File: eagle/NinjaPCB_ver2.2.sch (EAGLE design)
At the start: 58 parts, among them IC3 ANALOGSW_AD_SOT23-6, IC6 NAU7802, J2 ATX24, J3 HEATER, J4 HEATER_TEMP, Q1 S8550, Q2 IRF520NPBF, Q3 IRF520NPBF, Q4 S8550, Q5 IRF520NPBF, Q6 S8550, Q7 S8550, Q8 S8550, U1 CJT1117-3.3-SOT223

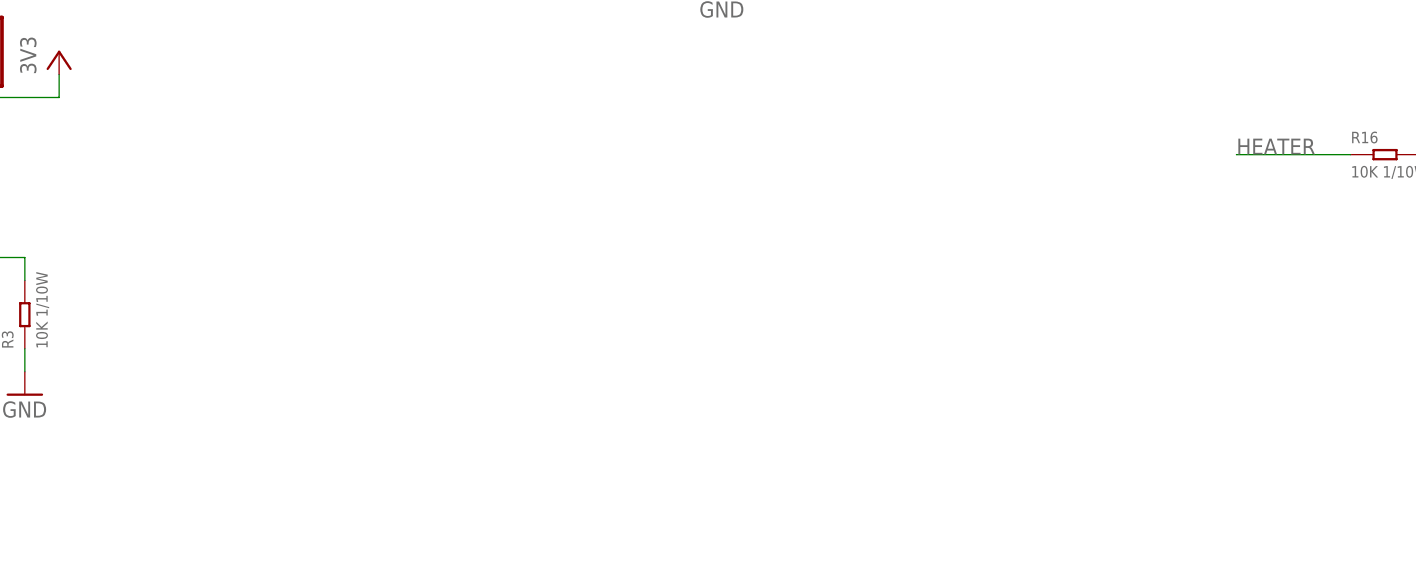
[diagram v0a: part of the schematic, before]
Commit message: changed R14 into RT. no reason for T
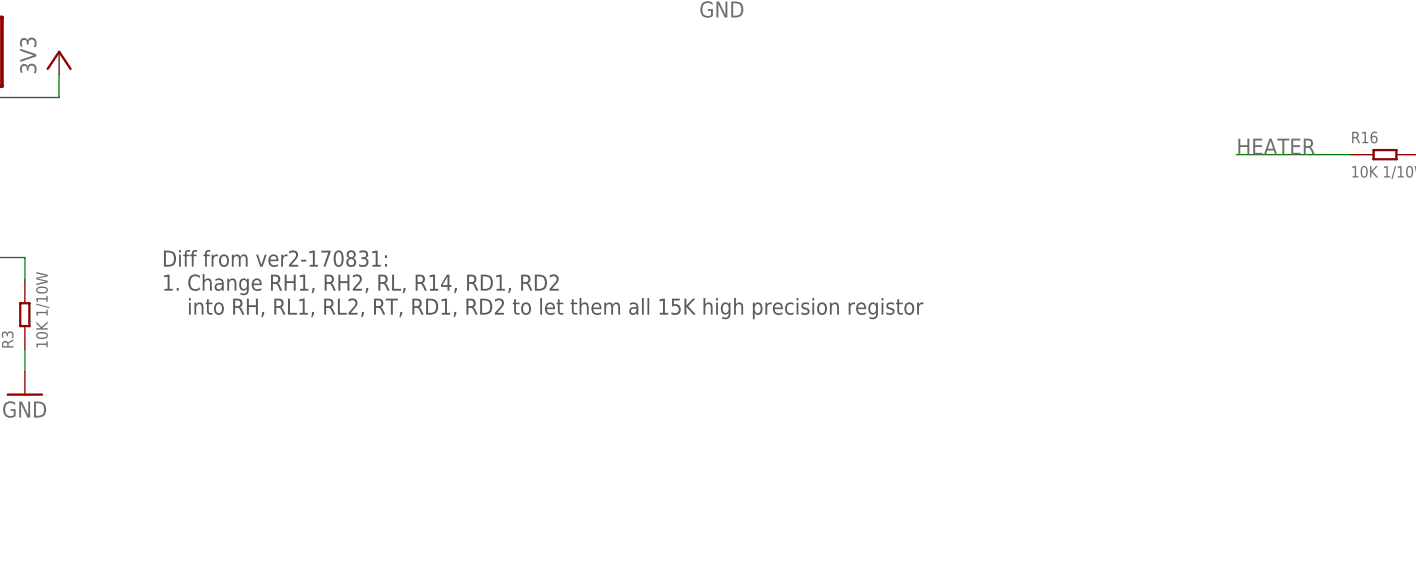
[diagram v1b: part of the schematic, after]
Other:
- note added: "Diff from ver2-170831: 1. Change RH1, RH2, RL, R14, RD1, RD2 into RH, RL1, RL2, RT, RD1, RD2 to let them all 15K high precision registor"
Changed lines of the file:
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@@
 <setting verticaltext="up"/>
 </settings>
-<grid distance="0.05" unitdist="inch" unit="inch" style="lines" multiple="1" display="no" altdistance="0.01" altunitdist="inch" altunit="inch"/>
+<grid distance="0.1" unitdist="inch" unit="inch" style="lines" multiple="1" display="no" altdistance="0.01" altunitdist="inch" altunit="inch"/>
 <layers>
 <layer number="1" name="Top" color="4" fill="1" visible="no" active="no"/>
@@
 <text x="26.67" y="238.76" size="3.81" layer="97">MCU</text>
 <text x="24.13" y="68.58" size="3.81" layer="97">POWER</text>
+<text x="167.64" y="91.44" size="1.778" layer="97">Diff from ver2-170831:
+1. Change RH1, RH2, RL, R14, RD1, RD2
+    into RH, RL1, RL2, RT, RD1, RD2 to let them all 15K high precision registor</text>
 </plain>
 <instances>
@@
 </schematic>
 </drawing>
+<compatibility>
+<note version="6.3" minversion="6.2.2" severity="warning">
+Since Version 6.2.2 text objects can contain more than one line,
+which will not be processed correctly with this version.
+</note>
+</compatibility>
 </eagle>

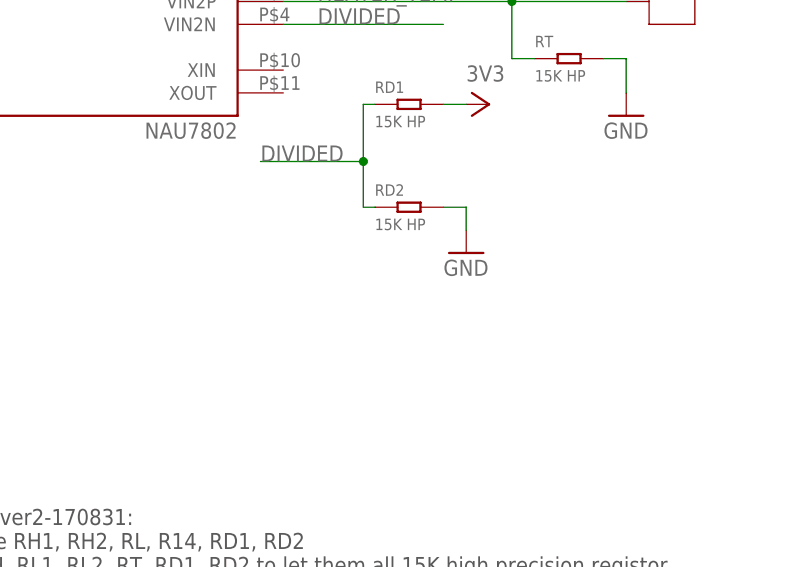
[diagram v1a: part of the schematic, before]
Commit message: add low ESR cap to standard voltage for NAU7802
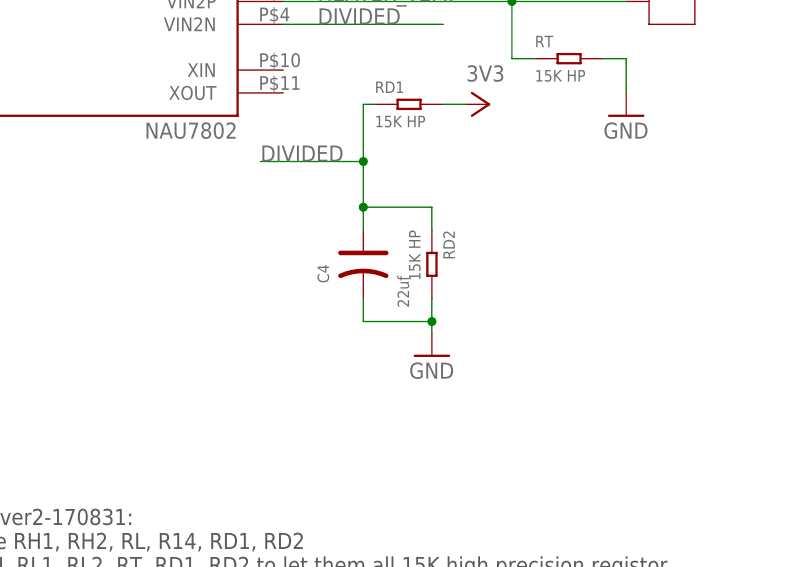
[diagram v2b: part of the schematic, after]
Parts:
- added C4: 22uf, Seeed-Capacitor:TANTALUM-SMD-22UF-16V(AVX-B)
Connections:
- net DIVIDED: now also C4.+
- net GND: now also C4.-
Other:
- moved on the sheet: RD2
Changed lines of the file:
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@@
 <setting verticaltext="up"/>
 </settings>
-<grid distance="0.1" unitdist="inch" unit="inch" style="lines" multiple="1" display="no" altdistance="0.01" altunitdist="inch" altunit="inch"/>
+<grid distance="0.05" unitdist="inch" unit="inch" style="lines" multiple="1" display="no" altdistance="0.01" altunitdist="inch" altunit="inch"/>
 <layers>
 <layer number="1" name="Top" color="4" fill="1" visible="no" active="no"/>
@@
 <part name="C1" library="Seeed-Capacitor" deviceset="CERAMIC-100NF-50V-10%-X7R(0603)" device="" value="100nf"/>
 <part name="RL1" library="PCR-RCL" deviceset="R0603" device="" value="15K HP"/>
+<part name="C4" library="Seeed-Capacitor" deviceset="TANTALUM-SMD-22UF-16V(AVX-B)" device="" value="22uf"/>
 </parts>
 <sheets>
@@
 <instance part="P+10" gate="VCC" x="214.63" y="177.8"/>
 <instance part="P+12" gate="VCC" x="232.41" y="143.51" rot="R270"/>
-<instance part="GND13" gate="1" x="229.87" y="127"/>
+<instance part="GND13" gate="1" x="226.06" y="115.57"/>
 <instance part="RD1" gate="G$1" x="223.52" y="143.51"/>
-<instance part="RD2" gate="G$1" x="223.52" y="132.08"/>
+<instance part="RD2" gate="G$1" x="226.06" y="125.73" rot="R270"/>
 <instance part="GND15" gate="1" x="160.02" y="135.89"/>
 <instance part="C3" gate="G$1" x="160.02" y="154.94" rot="R90"/>
@@
 <instance part="C1" gate="G$1" x="43.18" y="209.55"/>
 <instance part="RL1" gate="G$1" x="199.39" y="224.79"/>
+<instance part="C4" gate="G$1" x="218.44" y="125.73" smashed="yes" rot="R270">
+<attribute name="NAME" x="213.36" y="125.73" size="1.27" layer="95" ratio="10" rot="R270"/>
+<attribute name="VALUE" x="222.25" y="124.46" size="1.27" layer="96" ratio="10" rot="R270"/>
+</instance>
 </instances>
 <busses>
@@
 <segment>
 <pinref part="GND13" gate="1" pin="GND"/>
-<wire x1="229.87" y1="132.08" x2="229.87" y2="129.54" width="0.1524" layer="91"/>
 <pinref part="RD2" gate="G$1" pin="2"/>
-<wire x1="227.33" y1="132.08" x2="229.87" y2="132.08" width="0.1524" layer="91"/>
+<wire x1="226.06" y1="121.92" x2="226.06" y2="119.38" width="0.1524" layer="91"/>
+<pinref part="C4" gate="G$1" pin="-"/>
+<wire x1="226.06" y1="119.38" x2="226.06" y2="118.11" width="0.1524" layer="91"/>
+<wire x1="226.06" y1="119.38" x2="218.44" y2="119.38" width="0.1524" layer="91"/>
+<wire x1="218.44" y1="119.38" x2="218.44" y2="121.92" width="0.1524" layer="91"/>
+<junction x="226.06" y="119.38"/>
 </segment>
 <segment>
@@
 <label x="207.01" y="137.16" size="1.778" layer="95"/>
 <pinref part="RD2" gate="G$1" pin="1"/>
-<wire x1="219.71" y1="132.08" x2="218.44" y2="132.08" width="0.1524" layer="91"/>
-</segment>
-<segment>
+<wire x1="226.06" y1="129.54" x2="226.06" y2="132.08" width="0.1524" layer="91"/>
+<wire x1="226.06" y1="132.08" x2="218.44" y2="132.08" width="0.1524" layer="91"/>
+<pinref part="C4" gate="G$1" pin="+"/>
+<wire x1="218.44" y1="129.54" x2="218.44" y2="132.08" width="0.1524" layer="91"/>
+<junction x="218.44" y="132.08"/>
+</segment>
+<segment>

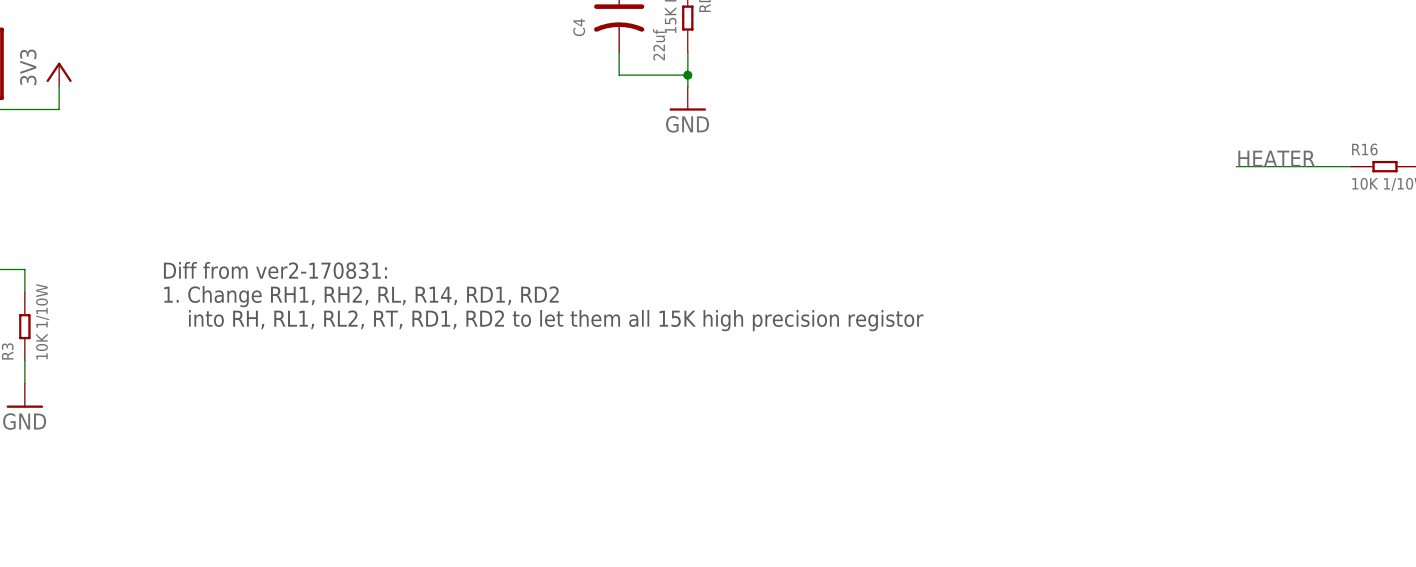
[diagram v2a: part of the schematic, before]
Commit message: add low ESR cap to standard voltage for NAU7802
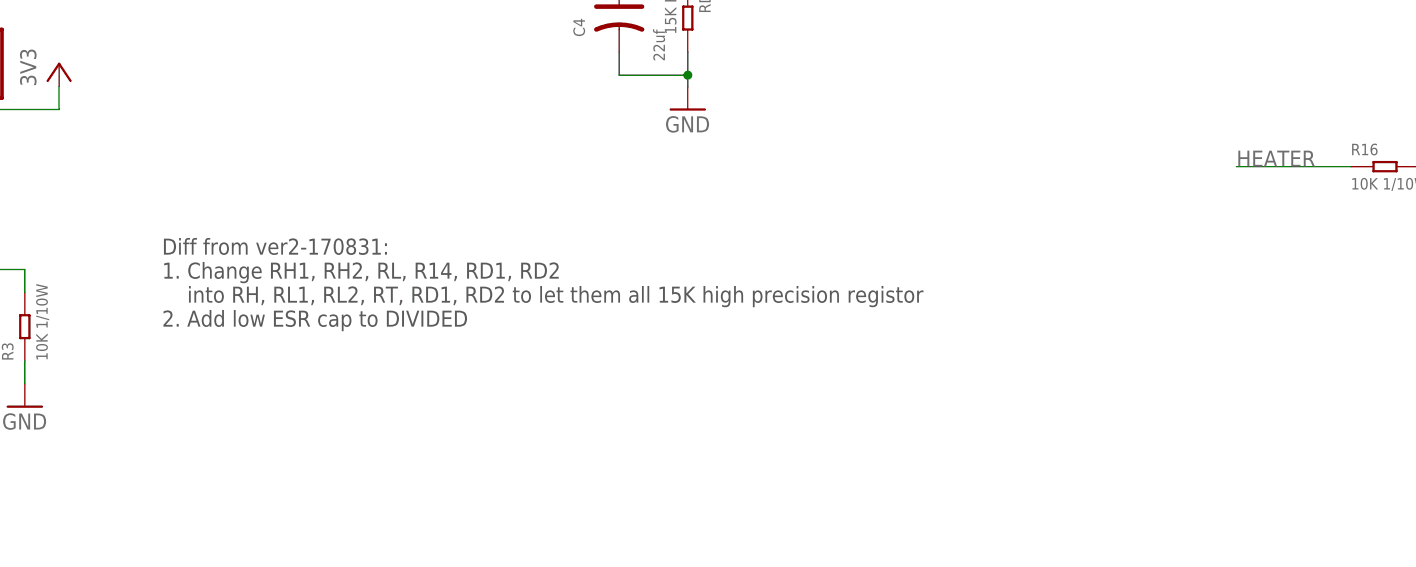
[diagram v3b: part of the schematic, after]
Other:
- note added: "Diff from ver2-170831: 1. Change RH1, RH2, RL, R14, RD1, RD2 into RH, RL1, RL2, RT, RD1, RD2 to let them all 15K high precision registor 2. Add low ESR cap to DIVIDED"
- note removed: "Diff from ver2-170831: 1. Change RH1, RH2, RL, R14, RD1, RD2 into RH, RL1, RL2, RT, RD1, RD2 to let them all 15K high precision registor"
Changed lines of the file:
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@@
 <text x="167.64" y="91.44" size="1.778" layer="97">Diff from ver2-170831:
 1. Change RH1, RH2, RL, R14, RD1, RD2
-    into RH, RL1, RL2, RT, RD1, RD2 to let them all 15K high precision registor</text>
+    into RH, RL1, RL2, RT, RD1, RD2 to let them all 15K high precision registor
+2. Add low ESR cap to DIVIDED</text>
 </plain>
 <instances>

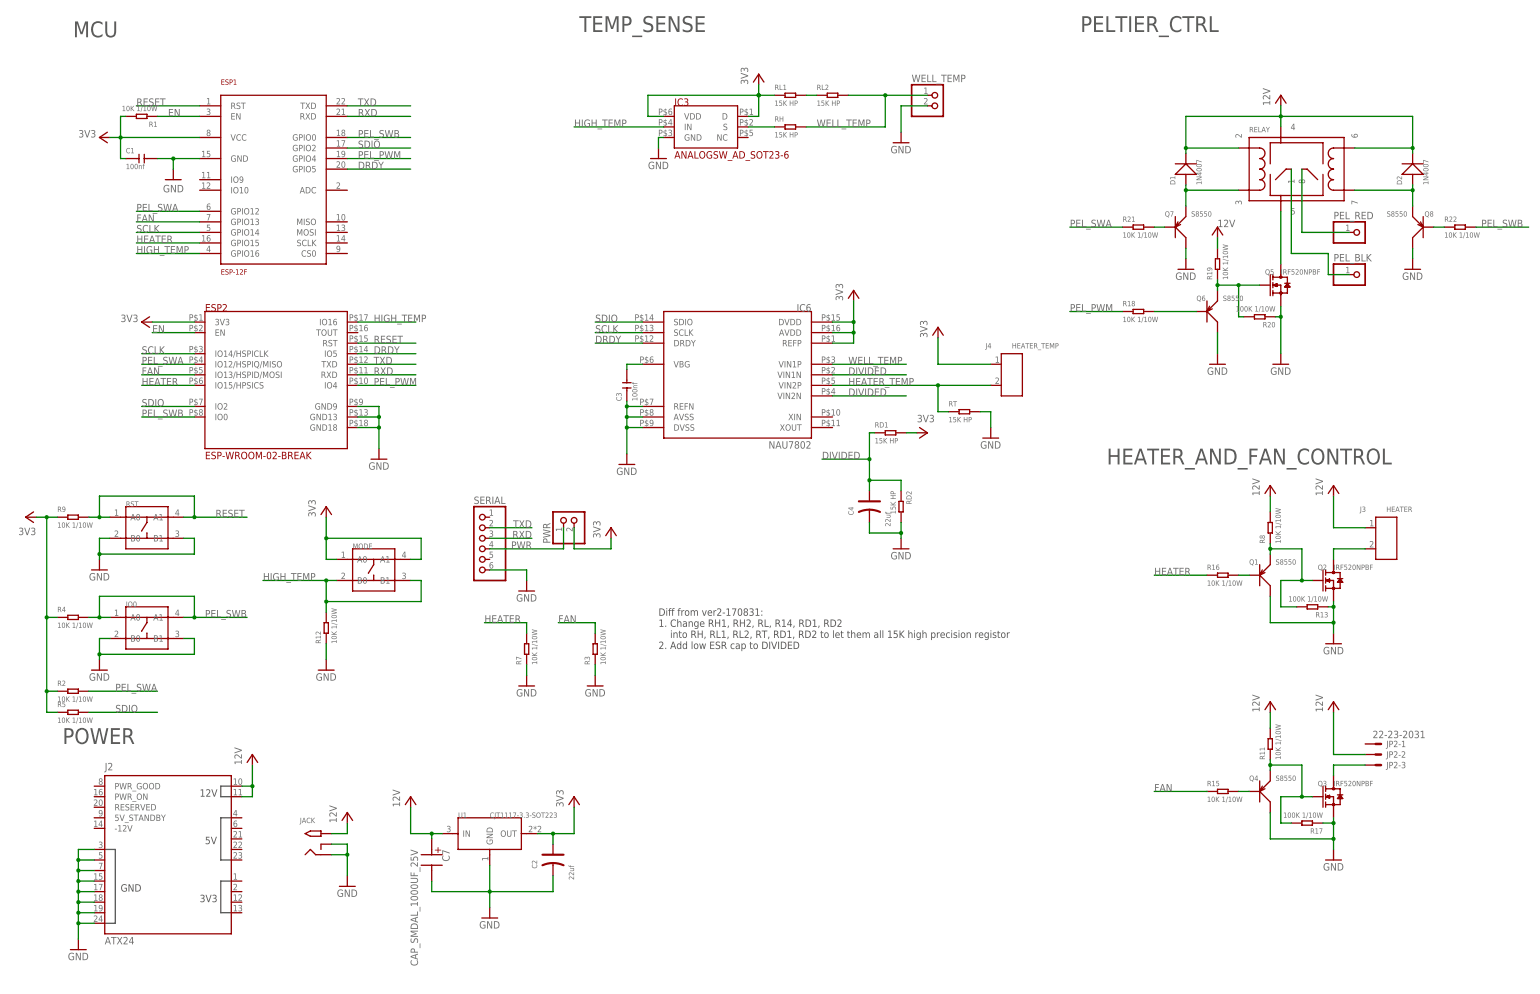
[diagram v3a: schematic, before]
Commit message: add low ESR cap to standard voltage for NAU7802
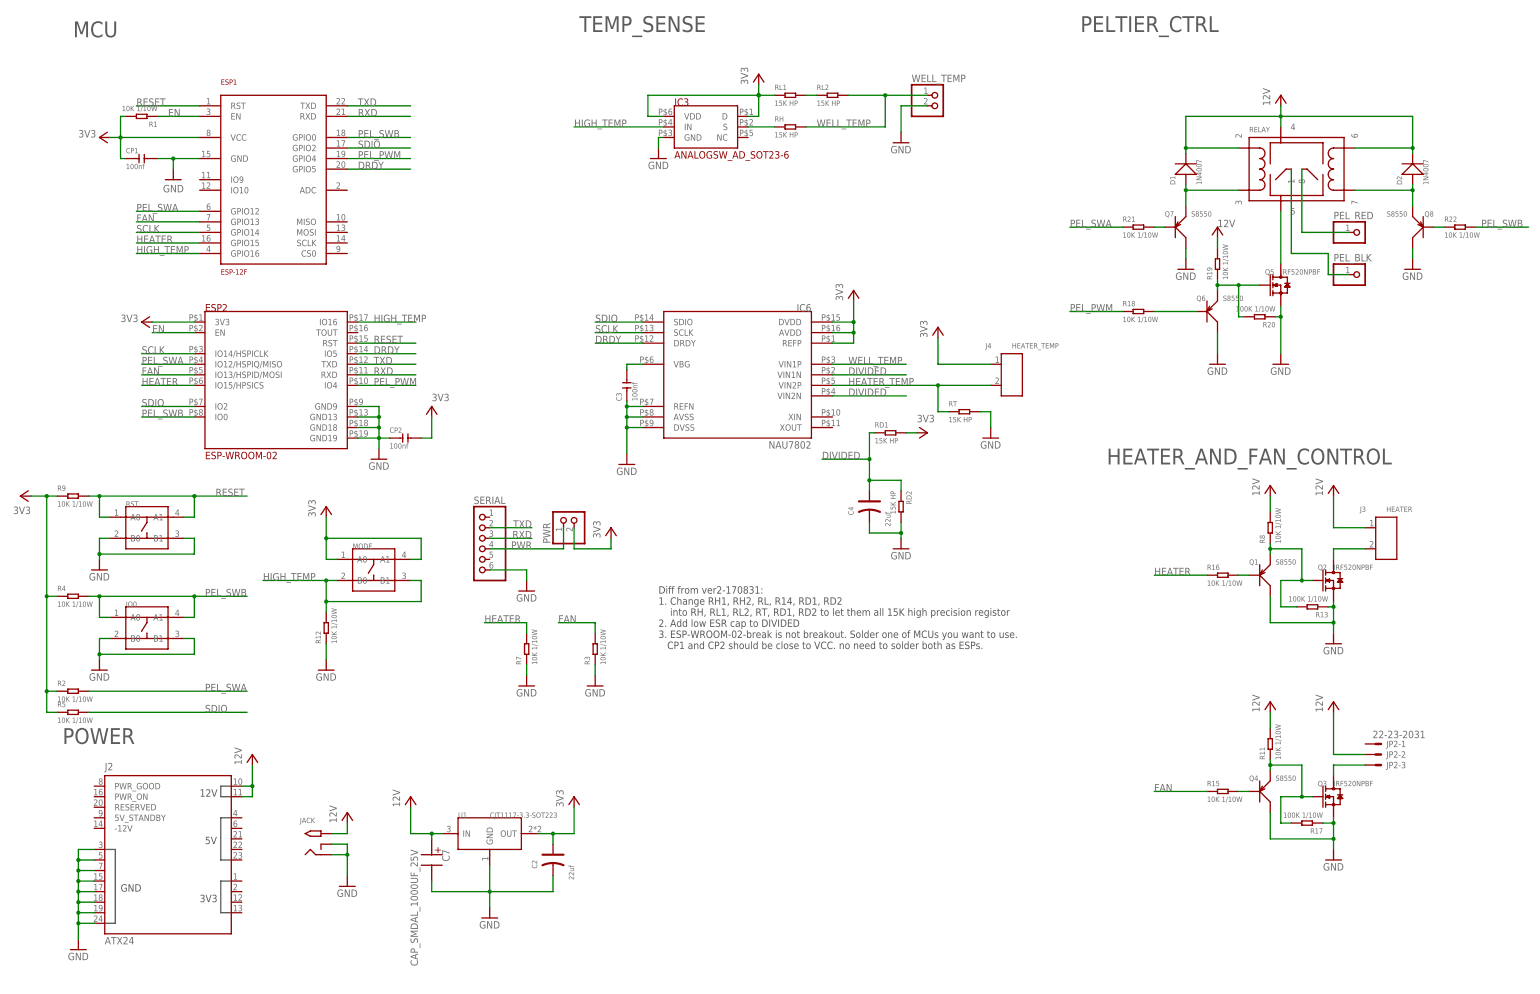
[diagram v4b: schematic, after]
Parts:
- added CP2: 100nf, Seeed-Capacitor:CERAMIC-100NF-50V-10%-X7R(0603)
- ESP2: value ESP-WROOM-02-BREAK -> ESP-WROOM-02; device PCR-Module:ESP-WROOM-02-BREAK -> PCR-Module:ESP-WROOM-02
- renumbered C1 to CP1
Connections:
- net 3V3: now also CP2.2
- net GND: now also CP2.1, ESP2.GND19
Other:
- note added: "Diff from ver2-170831: 1. Change RH1, RH2, RL, R14, RD1, RD2 into RH, RL1, RL2, RT, RD1, RD2 to let them all 15K high precision registor 2. Add low ESR cap to DIVIDED 3. ESP-WROOM-02-break is not breakout. Solder one of MCUs you want to use. CP1 and CP2 should be close to VCC. no need to solder both as ESPs."
- note removed: "Diff from ver2-170831: 1. Change RH1, RH2, RL, R14, RD1, RD2 into RH, RL1, RL2, RT, RD1, RD2 to let them all 15K high precision registor 2. Add low ESR cap to DIVIDED"
- moved on the sheet: R4, R9
